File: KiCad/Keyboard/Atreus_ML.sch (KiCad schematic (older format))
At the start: 85 parts, among them K1 CHERRY_ML, K10 CHERRY_ML, K11 CHERRY_ML, K12 CHERRY_ML, K13 CHERRY_ML, K14 CHERRY_ML, K15 CHERRY_ML, K16 CHERRY_ML, K17 CHERRY_ML, K18 CHERRY_ML, K19 CHERRY_ML, K2 CHERRY_ML, K20 CHERRY_ML, K21 CHERRY_ML, K22 CHERRY_ML, K23 CHERRY_ML, K24 CHERRY_ML, K25 CHERRY_ML, K26 CHERRY_ML, K27 CHERRY_ML, K28 CHERRY_ML, K29 CHERRY_ML, K3 CHERRY_ML, K30 CHERRY_ML, K31 CHERRY_ML, K32 CHERRY_ML, K33 CHERRY_ML, K34 CHERRY_ML, K35 CHERRY_ML, K36 CHERRY_ML, K37 CHERRY_ML, K38 CHERRY_ML, K39 CHERRY_ML, K4 CHERRY_ML, K40 CHERRY_ML, K41 CHERRY_ML, K42 CHERRY_ML, K5 CHERRY_ML, K6 CHERRY_ML, K7 CHERRY_ML, K8 CHERRY_ML, K9 CHERRY_ML, U1 TEENSY2.0-Compact

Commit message: Rev 2 is done
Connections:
- net at D22.2 (out), D23.2 (out), D24.2 (out)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: now also U1.28 (PB0); no longer U1.24 (PB7)
- net at D27.2 (out), D28.2 (out), D29.2 (out)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: now also U1.27 (PB1); no longer U1.28 (PB0)
- net at D31.2 (out), D32.2 (out), D33.2 (out)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: now also U1.26 (PB2); no longer U1.27 (PB1)
- net at D35.2 (out), D36.2 (out), D37.2 (out)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: now also U1.25 (PB3); no longer U1.26 (PB2)
- net at D39.2 (out), D40.2 (out), D41.2 (out)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: now also U1.24 (PB7); no longer U1.25 (PB3)
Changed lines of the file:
@@
 	6700 2050 7750 2050
 Wire Wire Line
-	9350 2100 9350 1750
-Wire Wire Line
-	10850 2100 9350 2100
-Wire Wire Line
 	9400 10000 11500 10000
 Wire Wire Line
@@
 	11300 1100 11150 1100
 Wire Wire Line
-	10650 1850 10650 750
+	10650 750  10650 1900
 Wire Wire Line
 	10650 750  15000 750
 Wire Wire Line
-	10700 1900 10700 800
+	10700 800  10700 1950
 Wire Wire Line
 	10700 800  14100 800
 Wire Wire Line
-	10750 1950 10750 850
+	10750 850  10750 2000
 Wire Wire Line
 	10750 850  13200 850
 Wire Wire Line
-	10800 2000 10800 900
+	10800 900  10800 2050
 Wire Wire Line
 	10800 900  12300 900
@@
 Connection ~ 11450 9450
 Wire Wire Line
-	9750 1850 10650 1850
-Wire Wire Line
-	9850 1900 10700 1900
-Wire Wire Line
-	9750 1850 9750 1750
-Wire Wire Line
-	9850 1900 9850 1750
-Wire Wire Line
-	10750 1950 9950 1950
-Wire Wire Line
-	9950 1950 9950 1750
-Wire Wire Line
-	10800 2000 10050 2000
-Wire Wire Line
-	10050 2000 10050 1750
+	10850 2100 10050 2100
+Wire Wire Line
+	10050 2100 10050 1750
+Wire Wire Line
+	10800 2050 9950 2050
+Wire Wire Line
+	9950 2050 9950 1750
+Wire Wire Line
+	10750 2000 9850 2000
+Wire Wire Line
+	9850 2000 9850 1750
+Wire Wire Line
+	10700 1950 9750 1950
+Wire Wire Line
+	9750 1950 9750 1750
+Wire Wire Line
+	10650 1900 9350 1900
+Wire Wire Line
+	9350 1900 9350 1750
 $EndSCHEMATC

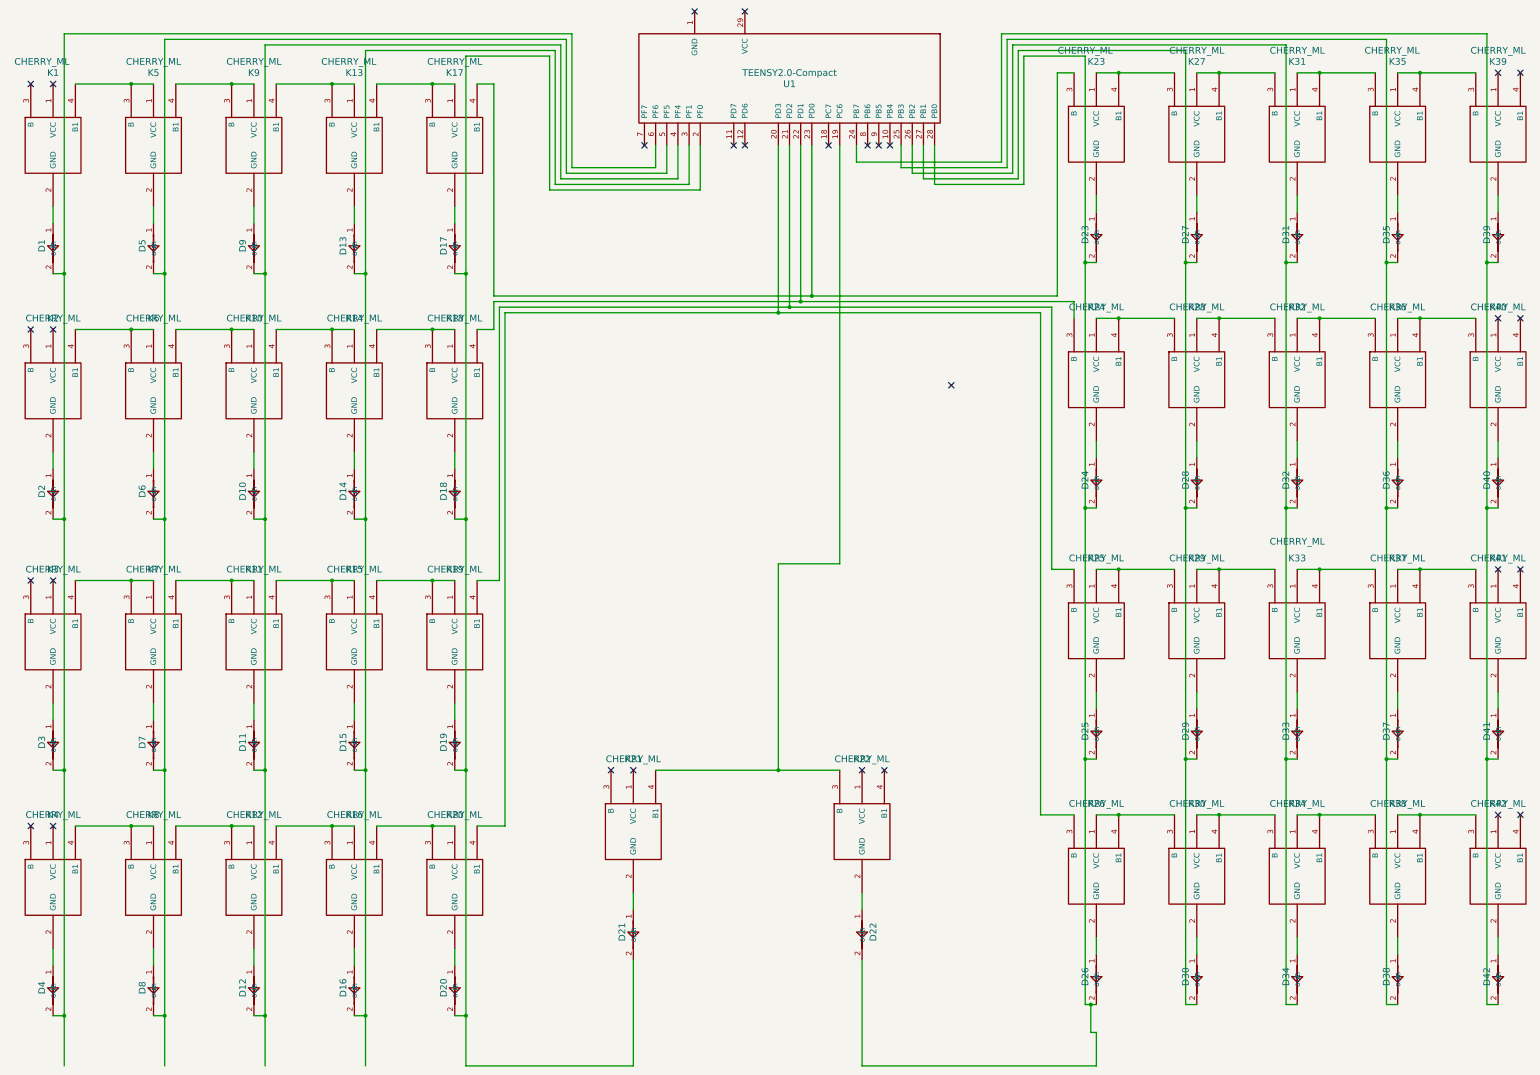
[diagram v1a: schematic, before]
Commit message: Rev 3, now with headers for unused pins
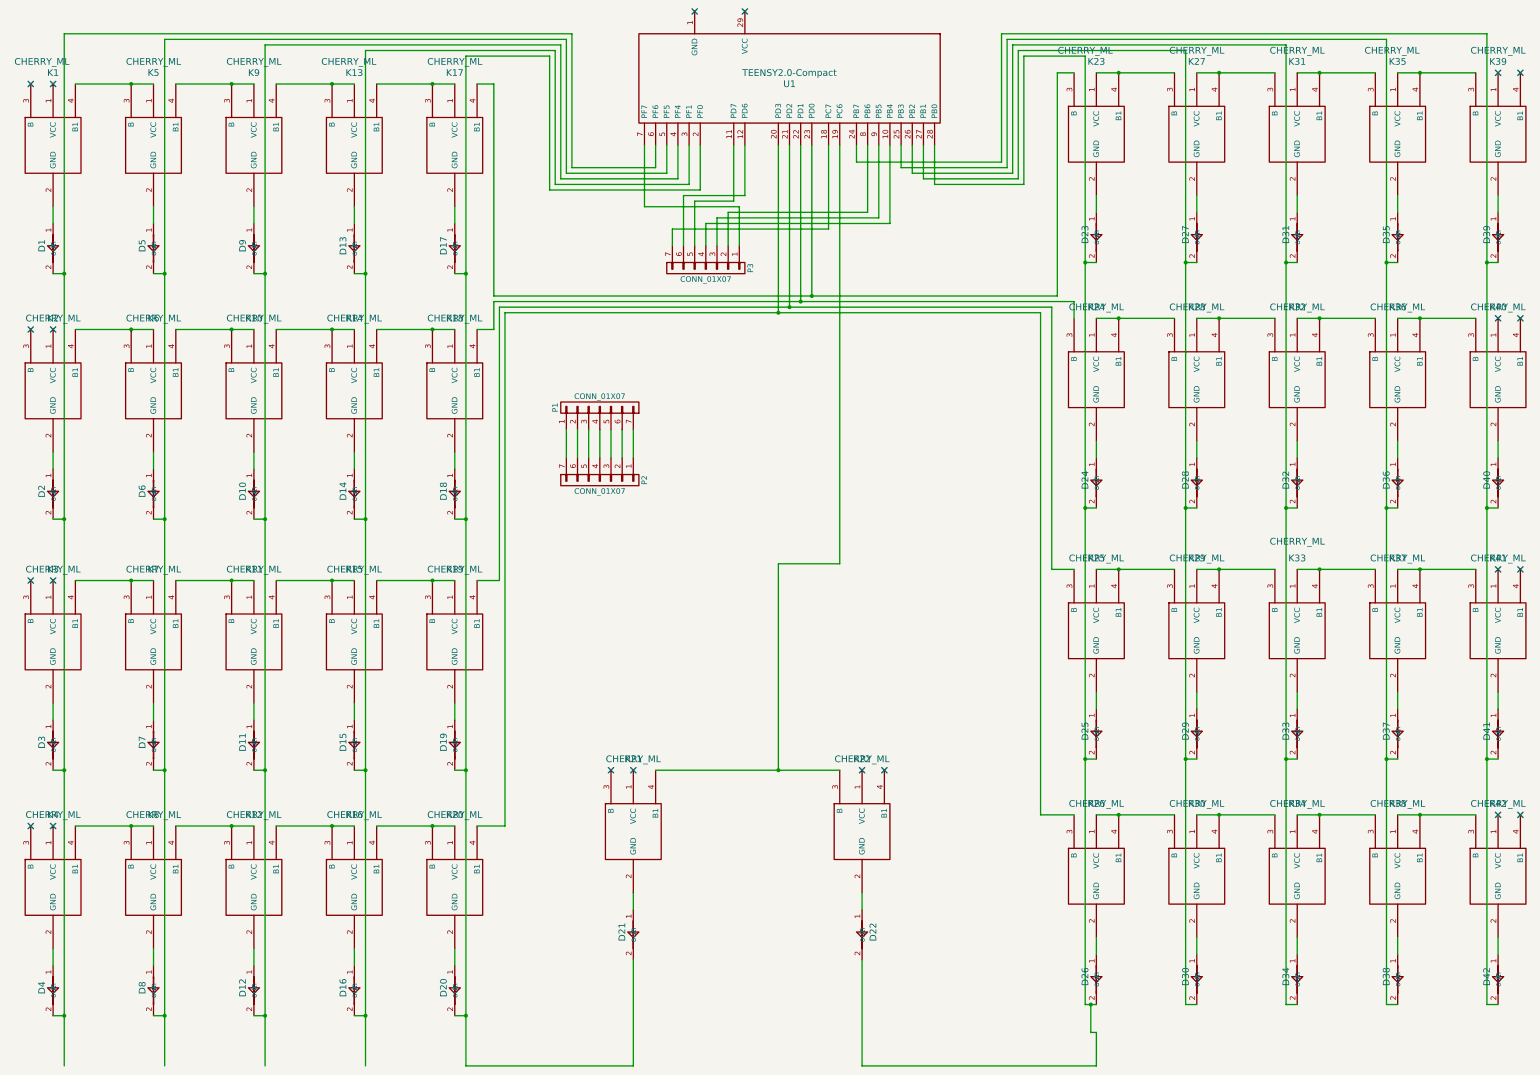
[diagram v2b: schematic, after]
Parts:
- added P1, P2, P3: CONN_01X07, Pin_Headers:Pin_Header_Straight_1x07, symbol CONN_01X07
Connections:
- net at U1.10 (PB4): now also P3.4 (P4)
- net at U1.11 (PD7): now also P3.5 (P5)
- net at U1.12 (PD6): now also P3.6 (P6)
- net at U1.18 (PC7): now also P3.7 (P7)
- net at U1.7 (PF7): now also P3.1 (P1)
- net at U1.8 (PB6): now also P3.2 (P2)
- net at U1.9 (PB5): now also P3.3 (P3)
- new net: P1.7 (P7), P2.1 (P1)
- new net: P1.6 (P6), P2.2 (P2)
- new net: P1.5 (P5), P2.3 (P3)
- new net: P1.4 (P4), P2.4 (P4)
- new net: P1.3 (P3), P2.5 (P5)
- new net: P1.2 (P2), P2.6 (P6)
- new net: P1.1 (P1), P2.7 (P7)
- no-connect marks 30 -> 22
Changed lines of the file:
@@
 LIBS:contrib
 LIBS:valves
-LIBS:4148_rev2
-LIBS:cherry_ml
 LIBS:components
 LIBS:Atreus_ML-cache
@@
 	0    1    1    0
 $EndComp
-NoConn ~ 9450 1750
-NoConn ~ 9550 1750
-NoConn ~ 9650 1750
-NoConn ~ 8350 1750
-NoConn ~ 8250 1750
-NoConn ~ 7450 1750
 NoConn ~ 7900 550
 NoConn ~ 8350 550
-NoConn ~ 9100 1750
-NoConn ~ 10200 3900
 $Comp
 L CHERRY_ML K22
@@
 	9400 10000 11500 10000
 Wire Wire Line
-	11000 7750 11000 3250
-Wire Wire Line
-	11300 7750 11000 7750
-Wire Wire Line
-	11100 5550 11100 3200
-Wire Wire Line
-	11300 5550 11100 5550
+	11000 3250 11000 7750
+Wire Wire Line
+	11000 7750 11300 7750
+Wire Wire Line
+	11100 3200 11100 5550
+Wire Wire Line
+	11100 5550 11300 5550
 Wire Wire Line
 	11300 3150 11300 3300
 Wire Wire Line
-	11150 1100 11150 3100
-Wire Wire Line
-	11300 1100 11150 1100
+	11150 3100 11150 1100
+Wire Wire Line
+	11150 1100 11300 1100
 Wire Wire Line
 	10650 750  10650 1900
@@
 Connection ~ 12300 5000
 Wire Wire Line
-	12400 5000 12300 5000
+	12300 5000 12400 5000
 Connection ~ 13200 5000
 Wire Wire Line
-	13300 5000 13200 5000
+	13200 5000 13300 5000
 Connection ~ 14100 5000
 Wire Wire Line
-	14200 5000 14100 5000
+	14100 5000 14200 5000
 Connection ~ 15000 5000
 Wire Wire Line
-	15100 5000 15000 5000
+	15000 5000 15100 5000
 Connection ~ 15000 7250
 Wire Wire Line
-	15100 7250 15000 7250
+	15000 7250 15100 7250
 Connection ~ 14100 7250
 Wire Wire Line
-	14200 7250 14100 7250
+	14100 7250 14200 7250
 Connection ~ 13200 7250
 Wire Wire Line
-	13300 7250 13200 7250
+	13200 7250 13300 7250
 Connection ~ 12300 7250
 Wire Wire Line
-	12400 7250 12300 7250
+	12300 7250 12400 7250
 Connection ~ 11400 7250
 Wire Wire Line
@@
 	12300 900  12300 9450
 Wire Wire Line
-	11500 9450 11400 9450
-Wire Wire Line
-	11400 9450 11400 950
+	11400 9450 11500 9450
+Wire Wire Line
+	11400 950  11400 9450
 Wire Wire Line
 	15100 8850 15100 9000
@@
 	6800 750  6800 1950
 Wire Wire Line
-	11100 3200 6150 3200
+	6150 3200 11100 3200
 Wire Wire Line
 	9400 9050 9400 10000
@@
 	5850 10000 7350 10000
 Wire Wire Line
-	11000 3250 6200 3250
+	6200 3250 11000 3250
 Wire Wire Line
 	6200 3250 6200 7850
@@
 	5950 3400 6100 3400
 Wire Wire Line
-	11150 3100 6100 3100
+	6100 3100 11150 3100
 Wire Wire Line
 	6100 3100 6100 1200
@@
 Connection ~ 5850 9550
 Wire Wire Line
-	5750 9550 5850 9550
+	5850 9550 5750 9550
 Connection ~ 4950 9550
 Wire Wire Line
-	4850 9550 4950 9550
+	4950 9550 4850 9550
 Connection ~ 4050 9550
 Wire Wire Line
-	3950 9550 4050 9550
+	4050 9550 3950 9550
 Connection ~ 3150 9550
 Wire Wire Line
-	3050 9550 3150 9550
+	3150 9550 3050 9550
 Connection ~ 2250 9550
 Wire Wire Line
-	2150 9550 2250 9550
+	2250 9550 2150 9550
 Connection ~ 5850 7350
 Wire Wire Line
-	5750 7350 5850 7350
+	5850 7350 5750 7350
 Connection ~ 4950 7350
 Wire Wire Line
-	4850 7350 4950 7350
+	4950 7350 4850 7350
 Connection ~ 4050 7350
 Wire Wire Line
-	3950 7350 4050 7350
+	4050 7350 3950 7350
 Connection ~ 3150 7350
 Wire Wire Line
-	3050 7350 3150 7350
+	3150 7350 3050 7350
 Connection ~ 2250 7350
 Wire Wire Line
-	2150 7350 2250 7350
+	2250 7350 2150 7350
 Connection ~ 5850 5100
 Wire Wire Line
-	5750 5100 5850 5100
+	5850 5100 5750 5100
 Connection ~ 4950 5100
 Wire Wire Line
-	4850 5100 4950 5100
+	4950 5100 4850 5100
 Connection ~ 4050 5100
 Wire Wire Line
-	3950 5100 4050 5100
+	4050 5100 3950 5100
 Connection ~ 5850 2900
 Wire Wire Line
@@
 Connection ~ 3150 5100
 Wire Wire Line
-	3050 5100 3150 5100
+	3150 5100 3050 5100
 Connection ~ 2250 5100
 Wire Wire Line
-	2150 5100 2250 5100
+	2250 5100 2150 5100
 Connection ~ 4950 2900
 Wire Wire Line
@@
 Wire Wire Line
 	9350 1900 9350 1750
+$Comp
+L CONN_01X07 P2
+U 1 1 56FCED09
+P 7050 4750
+F 0 "P2" H 7050 5150 50  0000 C CNN
+F 1 "CONN_01X07" V 7150 4750 50  0000 C CNN
+F 2 "Pin_Headers:Pin_Header_Straight_1x07" H 7050 4750 60  0001 C CNN
+F 3 "" H 7050 4750 60  0000 C CNN
+	1    7050 4750
+	0    1    1    0
+$EndComp
+$Comp
+L CONN_01X07 P1
+U 1 1 56FCF015
+P 7050 4100
+F 0 "P1" H 7050 4500 50  0000 C CNN
+F 1 "CONN_01X07" V 7150 4100 50  0000 C CNN
+F 2 "Pin_Headers:Pin_Header_Straight_1x07" H 7050 4100 60  0001 C CNN
+F 3 "" H 7050 4100 60  0000 C CNN
+	1    7050 4100
+	0    -1   -1   0
+$EndComp
+$Comp
+L CONN_01X07 P3
+U 1 1 56FCF1A7
+P 8000 2850
+F 0 "P3" H 8000 3250 50  0000 C CNN
+F 1 "CONN_01X07" V 8100 2850 50  0000 C CNN
+F 2 "Pin_Headers:Pin_Header_Straight_1x07" H 8000 2850 60  0001 C CNN
+F 3 "" H 8000 2850 60  0000 C CNN
+	1    8000 2850
+	0    1    1    0
+$EndComp
+Wire Wire Line
+	6750 4300 6750 4550
+Wire Wire Line
+	6850 4550 6850 4300
+Wire Wire Line
+	6950 4300 6950 4550
+Wire Wire Line
+	7050 4550 7050 4300
+Wire Wire Line
+	7150 4300 7150 4550
+Wire Wire Line
+	7250 4300 7250 4550
+Wire Wire Line
+	7350 4300 7350 4550
+Wire Wire Line
+	9100 1750 9100 2500
+Wire Wire Line
+	9100 2500 7700 2500
+Wire Wire Line
+	7700 2500 7700 2650
+Wire Wire Line
+	7450 1750 7450 2300
+Wire Wire Line
+	7450 2300 8300 2300
+Wire Wire Line
+	8300 2300 8300 2650
+Wire Wire Line
+	9450 1750 9450 2350
+Wire Wire Line
+	9450 2350 8200 2350
+Wire Wire Line
+	8200 2350 8200 2650
+Wire Wire Line
+	9550 1750 9550 2400
+Wire Wire Line
+	9550 2400 8100 2400
+Wire Wire Line
+	8100 2400 8100 2650
+Wire Wire Line
+	9650 1750 9650 2450
+Wire Wire Line
+	9650 2450 8000 2450
+Wire Wire Line
+	8000 2450 8000 2650
+Wire Wire Line
+	8250 1750 8250 2250
+Wire Wire Line
+	8250 2250 7900 2250
+Wire Wire Line
+	7900 2250 7900 2650
+Wire Wire Line
+	8350 1750 8350 2200
+Wire Wire Line
+	8350 2200 7800 2200
+Wire Wire Line
+	7800 2200 7800 2650
 $EndSCHEMATC

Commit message: Rev 4
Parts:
- K1, K10, K11, K12, K13, K14, K15, K16, K17, K18, K19, K2, K20, K21, K22, K23, K24, K25, K26, K27, K28, K29, K3, K30, K31, K32, K33, K34, K35, K36, K37, K38, K39, K4, K40, K41, K42, K5, K6, K7, K8, K9: footprint CHERRY_ML:CHERRY_ML -> Cherry_ML:CHERRY_ML_Etch
